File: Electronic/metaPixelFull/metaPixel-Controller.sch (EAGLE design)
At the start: 34 parts, among them IC1 74HCT14N, IC2 74HCT14N, IC3 74HCT74N, Q1 2N3906

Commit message: The first 3 Boards are ready
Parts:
- removed C10, C3, C4, C5, C6, C7, C8, C9: .1µ, rcl:C-EU025-024X044
- removed HOST: (no value), con-harting-ml:ML20L
- removed IC2: 74HCT14N, 74xx-eu:74HCT14N
- removed KEYBOARD: (no value), con-harting-ml:ML10L
- removed Q1: 2N3906, transistor-pnp:2N3906
- removed R10, R15, R6, R8: 82k, resistor:R-EU_0204/7
- removed R14, R5, R9: 15k, resistor:R-EU_0204/7
- removed R16, R17, R18, R19: 10k, resistor:R-EU_0204/7
- removed R20: 3k3, resistor:R-EU_0204/7
- added DC1: NME0505, dc-dc-converter:NME
- added OK1: 6N137, optocoupler:6N137
- added U$3: RP025-02, RP025xx:RP025-02
- added X3, X4: RIA_182_3, BlaBlub_USER:RIA_182_3
- C1, C2: value .1µ -> (none); device rcl:C-EU025-024X044 -> resistor:C-EU025-030X050
- IC1: value 74HCT14N -> MAX481CPA; device 74xx-eu:74HCT14N -> maxim:MAX481CPA
- IC3: value 74HCT74N -> 74HCT245N; device 74xx-eu:74HCT74N -> 74xx-eu:74HCT245N
- R1: value 10k -> 562; device resistor:R-EU_0204/7 -> resistor:R-EU_0207/7
- R2: value 100 -> 562; device resistor:R-EU_0204/7 -> resistor:R-EU_0207/7
- R3: value 15k -> 133; device resistor:R-EU_0204/7 -> resistor:R-EU_0207/7
- R4: value 82k -> 470; device resistor:R-EU_0204/7 -> rcl:R-EU_0207/10
- R7: value 15k -> 4k7; device resistor:R-EU_0204/7 -> resistor:R-EU_0207/10
- U$1: value 2.2_TFT_LCD -> TEENSY_3.1_OUTER_ROW; device 2.2"tft:2.2_TFT_LCD -> Teensy_3_and_LC_Series_Boards_v1.0:TEENSY_3.1_OUTER_ROW
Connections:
- removed net !LCD_CS: HOST.7, U$1.CS
- removed net !LCD_RST: HOST.2, U$1.RST
- removed net !MEM_CS: HOST.11, U$1.SD_CS
- removed net +5: HOST.3
- removed net BG_LED: Q1.C, U$1.LED
- removed net ENC1: C5.1, IC2B.I, R16.2
- removed net ENC2: C6.1, IC2A.I, R17.2
- removed net ENC_1: KEYBOARD.7, R16.1, R18.1
- removed net ENC_2: KEYBOARD.5, R17.1, R19.2
- removed net ENC_DIR: HOST.20, IC3A.Q
- removed net ENC_STEP: HOST.19, IC2A.O, IC3A.CLK
- removed net K1: C9.1, IC1A.I, R14.2
- removed net K2: C1.1, IC1B.I, R3.2
- removed net K3: C2.1, IC1C.I, R5.2
- removed net K4: C3.1, IC1E.I, R7.2
- removed net K5: C4.1, IC1D.I, R9.2
- removed net KEY_1: HOST.10, IC1A.O
- removed net KEY_2: HOST.12, IC1B.O
- removed net KEY_3: HOST.14, IC1C.O
- removed net KEY_4: HOST.16, IC1D.O
- removed net KEY_5: HOST.18, IC1E.O
- removed net K_1: KEYBOARD.4, R14.1, R15.1
- removed net K_2: KEYBOARD.6, R3.1, R4.1
- removed net K_3: KEYBOARD.8, R5.1, R6.1
- removed net K_4: KEYBOARD.10, R10.1, R9.1
- removed net K_5: KEYBOARD.9, R7.1, R8.1
- removed net LCD_DC: HOST.8, U$1.DC
- removed net LCD_LED: HOST.5, R2.1
- removed net MISO: HOST.9, U$1.MISO, U$1.SD_MISO
- removed net MOSI: HOST.4, U$1.MOSI, U$1.SD_MOSI
- removed net N$19: HOST.15
- removed net N$20: HOST.17
- removed net N$3: IC3A.CLR, IC3A.PRE, R20.2
- removed net SCLK: HOST.6, U$1.SCK, U$1.SD_SCK
- new net +5V_EXT: C1.1, DC1.+VOUT, IC1P.VCC, R1.2
- new net DMX+: IC1G$1.B, R1.1, R3.2, X3.1, X4.1
- new net DMX-: IC1G$1.A, R2.2, R3.1, X3.2, X4.2
- new net DMX_IN: OK1.VO, R7.1
- new net GND_EXT: C1.2, DC1.-VOUT, IC1G$1.DE, IC1G$1.RE/, IC1P.GND, OK1.C, R2.1, X3.3, X4.3
- new net LED_OUT: IC3A.B1
- new net LED_OUT3V: IC3A.A1
- new net VCC: C2.2, DC1.+VIN, IC3A.DIR, IC3P.VCC, OK1.VCC, OK1.VE, R7.2, U$1.VIN, U$3.P2
- net +3.3V: now also U$1.3.3V; no longer C10.1, C7.1, C8.1, HOST.13, IC1P.VCC, IC2P.VCC, IC3P.VCC, KEYBOARD.1, Q1.E, R1.1, R10.2, R15.2, R18.2, R19.1, R20.1, R4.2, R6.2, R8.2, U$1.VCC
- net GND: now also C2.1, DC1.-VIN, IC3A.G, OK1.GND, U$3.P1; no longer C1.2, C10.2, C2.2, C3.2, C4.2, C5.2, C6.2, C7.2, C8.2, C9.2, HOST.1, IC1P.GND, IC2P.GND, KEYBOARD.2
- net N$1: now also OK1.A, R4.1; no longer IC2B.O, IC3A.D
- net N$2: now also IC1G$1.RO, R4.2; no longer Q1.B, R1.2, R2.2
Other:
- note added: "CPU"
- note added: "DMX Input"

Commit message: the mainboard
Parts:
- removed U$3: RP025-02, RP025xx:RP025-02
- removed X3, X4: RIA_182_3, BlaBlub_USER:RIA_182_3
- added DMX_1, DMX_2: RP025-03, RP025xx:RP025-03
- added LED, POWER: RP025-02, RP025xx:RP025-02
- added SV1: HOST, con-harting-ml:ML20L
- C1, C2: value (none) -> 0.1µ
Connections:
- new net !LCD_CS: SV1.7, U$1.10/TX2/PWM
- new net !LCD_RST: SV1.2, U$1.2
- new net !SD_CS: SV1.11, U$1.21/A7/PWM
- new net ENC_DIR: SV1.20, U$1.20/A6/PWM
- new net ENC_STEP: SV1.19, U$1.19/A5/T/SCL0
- new net KEY_1: SV1.10, U$1.14/A0
- new net KEY_2: SV1.12, U$1.15/A1/T
- new net KEY_3: SV1.14, U$1.16/A2/T
- new net KEY_4: SV1.16, U$1.17/A3/T
- new net KEY_5: SV1.18, U$1.18/A4/T/SDA0
- new net LCD_DC: SV1.8, U$1.9/RX2/PWM
- new net LCD_LED: SV1.5, U$1.A14/DAC
- new net MISO: SV1.9, U$1.12/MISO
- new net MOSI: SV1.4, U$1.11/MOSI
- new net N$14: SV1.17
- new net N$15: SV1.15
- new net SCLK: SV1.6, U$1.13/SCK/LED
- net +3.3V: now also SV1.13
- net DMX+: now also DMX_1.P1, DMX_2.P1; no longer X3.1, X4.1
- net DMX-: now also DMX_1.P2, DMX_2.P2; no longer X3.2, X4.2
- net DMX_IN: now also U$1.0/RX1/T
- net GND: now also POWER.P2, SV1.1, U$1.AGND; no longer U$3.P1
- net GND_EXT: now also DMX_1.P3, DMX_2.P3, IC1G$1.DI; no longer X3.3, X4.3
- net LED_OUT: now also LED.P1, LED.P2
- net LED_OUT3V: now also U$1.4/CAN-RX-PWM
- net VCC: now also POWER.P1, SV1.3; no longer U$3.P2
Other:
- moved on the sheet: IC3

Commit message: Layout 1
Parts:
- IC2: value TEENSY_3.1_OUTER_ROW -> TEENSY_3.1
- renumbered U$1 to IC2
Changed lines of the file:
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@@
 <part name="IC3" library="74xx-eu" deviceset="74*245" device="N" technology="HCT"/>
 <part name="FRAME1" library="frames" deviceset="A3L-LOC" device="" value="Main"/>
-<part name="U$1" library="Teensy_3_and_LC_Series_Boards_v1.0" deviceset="TEENSY_3.1_OUTER_ROW" device=""/>
+<part name="IC2" library="Teensy_3_and_LC_Series_Boards_v1.0" deviceset="TEENSY_3.1_OUTER_ROW" device="" value="TEENSY_3.1"/>
 <part name="DMX" library="frames" deviceset="A3L-LOC" device="" value="P"/>
 <part name="C1" library="resistor" deviceset="C-EU" device="025-030X050" value="0.1µ"/>
@@
 <instance part="IC3" gate="A" x="238.76" y="177.8"/>
 <instance part="FRAME1" gate="G$1" x="0" y="0"/>
-<instance part="U$1" gate="G$1" x="119.38" y="165.1"/>
+<instance part="IC2" gate="G$1" x="119.38" y="165.1"/>
 <instance part="IC3" gate="P" x="342.9" y="124.46"/>
 <instance part="C2" gate="G$1" x="337.82" y="121.92" rot="R180"/>
@@
 </segment>
 <segment>
-<pinref part="U$1" gate="G$1" pin="GND"/>
+<pinref part="IC2" gate="G$1" pin="GND"/>
 <wire x1="142.24" y1="185.42" x2="152.4" y2="185.42" width="0.1524" layer="91"/>
 <label x="162.56" y="185.42" size="1.27" layer="95" xref="yes"/>
-<pinref part="U$1" gate="G$1" pin="AGND"/>
+<pinref part="IC2" gate="G$1" pin="AGND"/>
 <wire x1="152.4" y1="185.42" x2="162.56" y2="185.42" width="0.1524" layer="91"/>
 <wire x1="142.24" y1="172.72" x2="152.4" y2="172.72" width="0.1524" layer="91"/>
@@
 </segment>
 <segment>
-<pinref part="U$1" gate="G$1" pin="VIN"/>
+<pinref part="IC2" gate="G$1" pin="VIN"/>
 <wire x1="142.24" y1="193.04" x2="162.56" y2="193.04" width="0.1524" layer="91"/>
 <label x="162.56" y="193.04" size="1.27" layer="95" xref="yes"/>
@@
 </segment>
 <segment>
-<pinref part="U$1" gate="G$1" pin="4/CAN-RX-PWM"/>
+<pinref part="IC2" gate="G$1" pin="4/CAN-RX-PWM"/>
 <wire x1="96.52" y1="182.88" x2="78.74" y2="182.88" width="0.1524" layer="91"/>
 <label x="78.74" y="182.88" size="1.27" layer="95" rot="R180" xref="yes"/>
@@
 <net name="+3.3V" class="1">
 <segment>
-<pinref part="U$1" gate="G$1" pin="3.3V"/>
+<pinref part="IC2" gate="G$1" pin="3.3V"/>
 <wire x1="142.24" y1="190.5" x2="162.56" y2="190.5" width="0.1524" layer="91"/>
 <label x="162.56" y="190.5" size="1.27" layer="95" xref="yes"/>
@@
 <net name="DMX_IN" class="1">
 <segment>
-<pinref part="U$1" gate="G$1" pin="0/RX1/T"/>
+<pinref part="IC2" gate="G$1" pin="0/RX1/T"/>
 <wire x1="96.52" y1="193.04" x2="78.74" y2="193.04" width="0.1524" layer="91"/>
 <label x="78.74" y="193.04" size="1.27" layer="95" rot="R180" xref="yes"/>
@@
 <net name="!LCD_RST" class="0">
 <segment>
-<pinref part="U$1" gate="G$1" pin="2"/>
+<pinref part="IC2" gate="G$1" pin="2"/>
 <wire x1="96.52" y1="187.96" x2="78.74" y2="187.96" width="0.1524" layer="91"/>
 <label x="78.74" y="187.96" size="1.27" layer="95" rot="R180" xref="yes"/>
@@
 <net name="LCD_DC" class="0">
 <segment>
-<pinref part="U$1" gate="G$1" pin="9/RX2/PWM"/>
+<pinref part="IC2" gate="G$1" pin="9/RX2/PWM"/>
 <wire x1="96.52" y1="170.18" x2="78.74" y2="170.18" width="0.1524" layer="91"/>
 <label x="78.74" y="170.18" size="1.27" layer="95" rot="R180" xref="yes"/>
@@
 <net name="!LCD_CS" class="0">
 <segment>
-<pinref part="U$1" gate="G$1" pin="10/TX2/PWM"/>
+<pinref part="IC2" gate="G$1" pin="10/TX2/PWM"/>
 <wire x1="96.52" y1="167.64" x2="78.74" y2="167.64" width="0.1524" layer="91"/>
 <label x="78.74" y="167.64" size="1.27" layer="95" rot="R180" xref="yes"/>
@@
 <net name="MOSI" class="0">
 <segment>
-<pinref part="U$1" gate="G$1" pin="11/MOSI"/>
+<pinref part="IC2" gate="G$1" pin="11/MOSI"/>
 <wire x1="96.52" y1="165.1" x2="78.74" y2="165.1" width="0.1524" layer="91"/>
 <label x="78.74" y="165.1" size="1.27" layer="95" rot="R180" xref="yes"/>
@@
 <net name="MISO" class="0">
 <segment>
-<pinref part="U$1" gate="G$1" pin="12/MISO"/>
+<pinref part="IC2" gate="G$1" pin="12/MISO"/>
 <wire x1="96.52" y1="162.56" x2="78.74" y2="162.56" width="0.1524" layer="91"/>
 <label x="78.74" y="162.56" size="1.27" layer="95" rot="R180" xref="yes"/>
@@
 <net name="SCLK" class="0">
 <segment>
-<pinref part="U$1" gate="G$1" pin="13/SCK/LED"/>
+<pinref part="IC2" gate="G$1" pin="13/SCK/LED"/>
 <wire x1="96.52" y1="160.02" x2="78.74" y2="160.02" width="0.1524" layer="91"/>
 <label x="78.74" y="160.02" size="1.27" layer="95" rot="R180" xref="yes"/>
@@
 <net name="LCD_LED" class="0">
 <segment>
-<pinref part="U$1" gate="G$1" pin="A14/DAC"/>
+<pinref part="IC2" gate="G$1" pin="A14/DAC"/>
 <wire x1="142.24" y1="167.64" x2="162.56" y2="167.64" width="0.1524" layer="91"/>
 <label x="162.56" y="167.64" size="1.27" layer="95" xref="yes"/>
@@
 <net name="!SD_CS" class="0">
 <segment>
-<pinref part="U$1" gate="G$1" pin="21/A7/PWM"/>
+<pinref part="IC2" gate="G$1" pin="21/A7/PWM"/>
 <wire x1="96.52" y1="139.7" x2="78.74" y2="139.7" width="0.1524" layer="91"/>
 <label x="78.74" y="139.7" size="1.27" layer="95" rot="R180" xref="yes"/>
@@
 <net name="KEY_1" class="0">
 <segment>
-<pinref part="U$1" gate="G$1" pin="14/A0"/>
+<pinref part="IC2" gate="G$1" pin="14/A0"/>
 <wire x1="96.52" y1="157.48" x2="78.74" y2="157.48" width="0.1524" layer="91"/>
 <label x="78.74" y="157.48" size="1.27" layer="95" rot="R180" xref="yes"/>
@@
 <net name="KEY_2" class="0">
 <segment>
-<pinref part="U$1" gate="G$1" pin="15/A1/T"/>
+<pinref part="IC2" gate="G$1" pin="15/A1/T"/>
 <wire x1="78.74" y1="154.94" x2="96.52" y2="154.94" width="0.1524" layer="91"/>
 <label x="78.74" y="154.94" size="1.27" layer="95" rot="R180" xref="yes"/>
@@
 <net name="KEY_3" class="0">
 <segment>
-<pinref part="U$1" gate="G$1" pin="16/A2/T"/>
+<pinref part="IC2" gate="G$1" pin="16/A2/T"/>
 <wire x1="96.52" y1="152.4" x2="78.74" y2="152.4" width="0.1524" layer="91"/>
 <label x="78.74" y="152.4" size="1.27" layer="95" rot="R180" xref="yes"/>
@@
 <net name="KEY_4" class="0">
 <segment>
-<pinref part="U$1" gate="G$1" pin="17/A3/T"/>
+<pinref part="IC2" gate="G$1" pin="17/A3/T"/>
 <wire x1="78.74" y1="149.86" x2="96.52" y2="149.86" width="0.1524" layer="91"/>
 <label x="78.74" y="149.86" size="1.27" layer="95" rot="R180" xref="yes"/>
@@
 <net name="KEY_5" class="0">
 <segment>
-<pinref part="U$1" gate="G$1" pin="18/A4/T/SDA0"/>
+<pinref part="IC2" gate="G$1" pin="18/A4/T/SDA0"/>
 <wire x1="96.52" y1="147.32" x2="78.74" y2="147.32" width="0.1524" layer="91"/>
 <label x="78.74" y="147.32" size="1.27" layer="95" rot="R180" xref="yes"/>
@@
 <net name="ENC_STEP" class="0">
 <segment>
-<pinref part="U$1" gate="G$1" pin="19/A5/T/SCL0"/>
+<pinref part="IC2" gate="G$1" pin="19/A5/T/SCL0"/>
 <wire x1="78.74" y1="144.78" x2="96.52" y2="144.78" width="0.1524" layer="91"/>
 <label x="78.74" y="144.78" size="1.27" layer="95" rot="R180" xref="yes"/>
@@
 <net name="ENC_DIR" class="0">
 <segment>
-<pinref part="U$1" gate="G$1" pin="20/A6/PWM"/>
+<pinref part="IC2" gate="G$1" pin="20/A6/PWM"/>
 <wire x1="96.52" y1="142.24" x2="78.74" y2="142.24" width="0.1524" layer="91"/>
 <label x="78.74" y="142.24" size="1.27" layer="95" rot="R180" xref="yes"/>

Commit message: boards
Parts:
- SV1: value HOST -> DISPLAY
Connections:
- removed net N$14: SV1.17
- removed net N$15: SV1.15
- net GND: no longer IC2.AGND
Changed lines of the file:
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@@
 <part name="SUPPLY2" library="supply2" deviceset="VCC" device=""/>
 <part name="POWER" library="RP025xx" deviceset="RP025-02" device=""/>
-<part name="SV1" library="con-harting-ml" deviceset="ML20" device="L" value="HOST"/>
+<part name="SV1" library="con-harting-ml" deviceset="ML20" device="L" value="DISPLAY"/>
 <part name="DMX_1" library="RP025xx" deviceset="RP025-03" device=""/>
 <part name="DMX_2" library="RP025xx" deviceset="RP025-03" device=""/>
@@
 <segment>
 <pinref part="IC2" gate="G$1" pin="GND"/>
-<wire x1="142.24" y1="185.42" x2="152.4" y2="185.42" width="0.1524" layer="91"/>
 <label x="162.56" y="185.42" size="1.27" layer="95" xref="yes"/>
-<pinref part="IC2" gate="G$1" pin="AGND"/>
-<wire x1="152.4" y1="185.42" x2="162.56" y2="185.42" width="0.1524" layer="91"/>
-<wire x1="142.24" y1="172.72" x2="152.4" y2="172.72" width="0.1524" layer="91"/>
-<wire x1="152.4" y1="172.72" x2="152.4" y2="185.42" width="0.1524" layer="91"/>
-<junction x="152.4" y="185.42"/>
+<wire x1="142.24" y1="185.42" x2="162.56" y2="185.42" width="0.1524" layer="91"/>
 </segment>
 <segment>
@@
 </segment>
 </net>
-<net name="LED_OUT" class="0">
+<net name="LED_OUT" class="1">
 <segment>
 <pinref part="IC3" gate="A" pin="B1"/>
@@
 </segment>
 </net>
-<net name="N$14" class="0">
-<segment>
-<pinref part="SV1" gate="1" pin="17"/>
-<wire x1="254" y1="116.84" x2="238.76" y2="116.84" width="0.1524" layer="91"/>
-<label x="254" y="116.84" size="1.27" layer="95" xref="yes"/>
-</segment>
-</net>
-<net name="N$15" class="0">
-<segment>
-<pinref part="SV1" gate="1" pin="15"/>
-<wire x1="238.76" y1="114.3" x2="254" y2="114.3" width="0.1524" layer="91"/>
-<label x="254" y="114.3" size="1.27" layer="95" xref="yes"/>
-</segment>
-</net>

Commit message: Fixing the boards
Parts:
- removed POWER: RP025-02, RP025xx:RP025-02
- removed SV1: DISPLAY, con-harting-ml:ML20L
- added J1: PWR, SparkFun-Connectors:POWER_JACKSLT
- added PWR: RP025-02, RP025xx:RP025-02
- added SK1: Display, jt-con-micromatch:MMATCH-20-PTH
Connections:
- removed net !SD_CS: IC2.21/A7/PWM, SV1.11
- removed net ENC_DIR: IC2.20/A6/PWM, SV1.20
- removed net ENC_STEP: IC2.19/A5/T/SCL0, SV1.19
- new net !MEM_CS: IC2.21/A7/PWM, SK1.13
- new net ENC_A: IC2.14/A0, SK1.14
- new net ENC_B: IC2.15/A1/T, SK1.15
- net !LCD_CS: now also SK1.6; no longer SV1.7
- net !LCD_RST: now also SK1.7; no longer SV1.2
- net +3.3V: now also SK1.17, SK1.19; no longer SV1.13
- net GND: now also J1.GNDBREAK, PWR.P2, SK1.16, SK1.18, SK1.20; no longer POWER.P2, SV1.1
- net KEY_1: now also IC2.20/A6/PWM, SK1.1; no longer IC2.14/A0, SV1.10
- net KEY_2: now also IC2.19/A5/T/SCL0, SK1.2; no longer IC2.15/A1/T, SV1.12
- net KEY_3: now also IC2.18/A4/T/SDA0, SK1.3; no longer IC2.16/A2/T, SV1.14
- net KEY_4: now also SK1.4; no longer SV1.16
- net KEY_5: now also IC2.16/A2/T, SK1.5; no longer IC2.18/A4/T/SDA0, SV1.18
- net LCD_DC: now also SK1.8; no longer SV1.8
- net LCD_LED: now also SK1.11; no longer SV1.5
- net LED_OUT: no longer LED.P2
- net MISO: now also SK1.12; no longer SV1.9
- net MOSI: now also SK1.9; no longer SV1.4
- net SCLK: now also SK1.10; no longer SV1.6
- net VCC: now also J1.PWR, PWR.P1; no longer POWER.P1, SV1.3

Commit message: fixing TFT_LED problem
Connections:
- net LCD_LED: now also IC2.6/PWM; no longer IC2.A14/DAC
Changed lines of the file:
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@@
 <net name="LCD_LED" class="0">
-<segment>
-<pinref part="IC2" gate="G$1" pin="A14/DAC"/>
-<wire x1="142.24" y1="167.64" x2="162.56" y2="167.64" width="0.1524" layer="91"/>
-<label x="162.56" y="167.64" size="1.27" layer="95" xref="yes"/>
-</segment>
 <segment>
 <pinref part="SK1" gate="G$1" pin="11"/>
@@
 <label x="215.9" y="99.06" size="1.27" layer="95" rot="R180" xref="yes"/>
 </segment>
+<segment>
+<pinref part="IC2" gate="G$1" pin="6/PWM"/>
+<wire x1="96.52" y1="177.8" x2="78.74" y2="177.8" width="0.1524" layer="91"/>
+<label x="78.74" y="177.8" size="1.27" layer="95" rot="R180" xref="yes"/>
+</segment>
 </net>

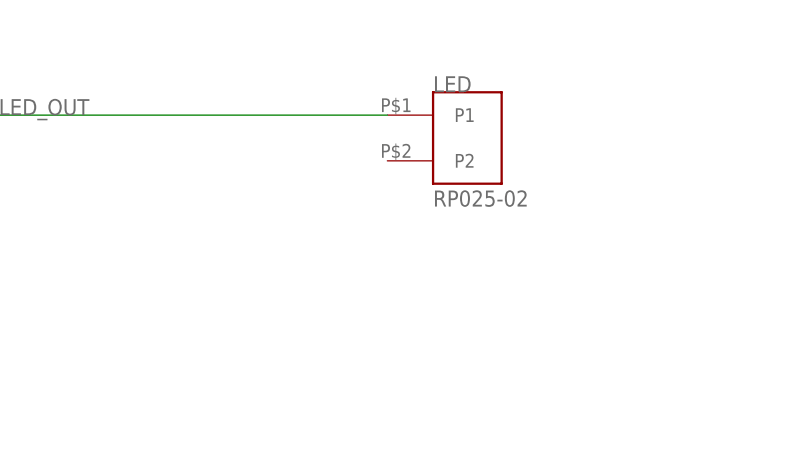
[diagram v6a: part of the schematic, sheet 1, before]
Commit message: added some warning if module dimensions are not set
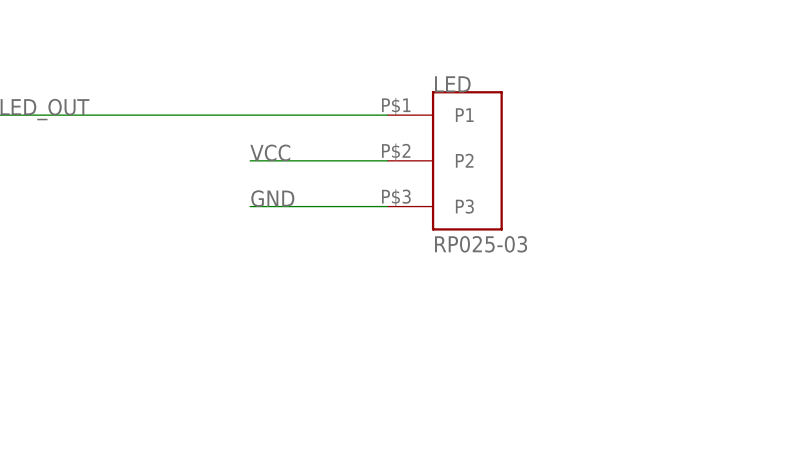
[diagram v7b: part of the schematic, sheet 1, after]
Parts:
- LED: value RP025-02 -> RP025-03; device RP025xx:RP025-02 -> RP025xx:RP025-03
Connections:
- net GND: now also LED.P3
- net VCC: now also LED.P2
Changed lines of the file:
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@@
 <?xml version="1.0" encoding="utf-8"?>
 <!DOCTYPE eagle SYSTEM "eagle.dtd">
-<eagle version="7.5.0">
+<eagle version="8.3.1">
 <drawing>
 <settings>
 <setting alwaysvectorfont="yes"/>
+<setting keepoldvectorfont="yes"/>
 <setting verticaltext="up"/>
 </settings>
@@
 <part name="DMX_1" library="RP025xx" deviceset="RP025-03" device=""/>
 <part name="DMX_2" library="RP025xx" deviceset="RP025-03" device=""/>
-<part name="LED" library="RP025xx" deviceset="RP025-02" device=""/>
+<part name="LED" library="RP025xx" deviceset="RP025-03" device=""/>
 <part name="J1" library="SparkFun-Connectors" deviceset="POWER_JACK" device="SLT" value="PWR"/>
 <part name="SK1" library="jt-con-micromatch" deviceset="MMATCH-20-*" device="PTH" value="Display"/>
@@
 <junction x="246.38" y="104.14"/>
 </segment>
+<segment>
+<pinref part="LED" gate="G$1" pin="P3"/>
+<wire x1="297.18" y1="180.34" x2="281.94" y2="180.34" width="0.1524" layer="91"/>
+<label x="281.94" y="180.34" size="1.778" layer="95"/>
+</segment>
 </net>
 <net name="VCC" class="1">
@@
 <label x="71.12" y="91.44" size="1.27" layer="95" xref="yes"/>
 </segment>
+<segment>
+<pinref part="LED" gate="G$1" pin="P2"/>
+<wire x1="297.18" y1="185.42" x2="281.94" y2="185.42" width="0.1524" layer="91"/>
+<label x="281.94" y="185.42" size="1.778" layer="95"/>
+</segment>
 </net>
